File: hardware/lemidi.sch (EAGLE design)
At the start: 70 parts, among them Q1 IRLML6246, Q2 IRLML6246, Q3 IRLML6246, Q4 IRLML6246, Q5 si2305cd, U1 SPX5205 3v3, X3 debug, Y2 12MHz 0.25%, Y3 8MHz

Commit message: max5415
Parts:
- removed U$11: SJ_3P, Simplex-Jumpers:SJ_3P
- added C22: 100nF, rcl:C-EUC0805
- added J1: SJ_3P, Simplex-Jumpers:SJ_3P
- C18: value 100nF -> 1uF
- C19: value 4.7uF -> 100nF
- C2, C5: value 22pF -> 27pF
- R10, R6, R9: value 100k -> 47K
- U$9: value UBA-4R-D14T-4D -> USB-A
- Y2: value 12MHz 0.25% -> 12MHz 0.25% CL 16pF
- Y3: value 8MHz -> 8MHz CL 18pF
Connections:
- net TP5 renamed CS_J1
- removed net USB_ST1: R9.1, U$3.GPOUT3
- removed net USB_ST2: R10.1, U$3.GPOUT4
- removed net USB_ST3: R6.1, U$3.GPOUT2
- new net STATUS1: R6.1, U$3.GPOUT6
- new net STATUS2: R9.1, U$3.GPOUT7
- net +5V: now also C22.2, J1.2; no longer U$11.2
- net 5V_PC: now also U$10.15, U$10.8; no longer U$10.1, U$10.9
- net 5V_PC2: now also U$10.1, U$10.9; no longer U$10.15, U$10.8
- net GND: now also C22.1
- net N$10: now also J1.1; no longer U$11.1
- net N$23: now also J1.3; no longer U$11.3
- net SCLK: now also R10.1
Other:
- moved on the sheet: C1, C11, C12, C13, C14, C15, C16, C17, C18, C19, C20, C21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

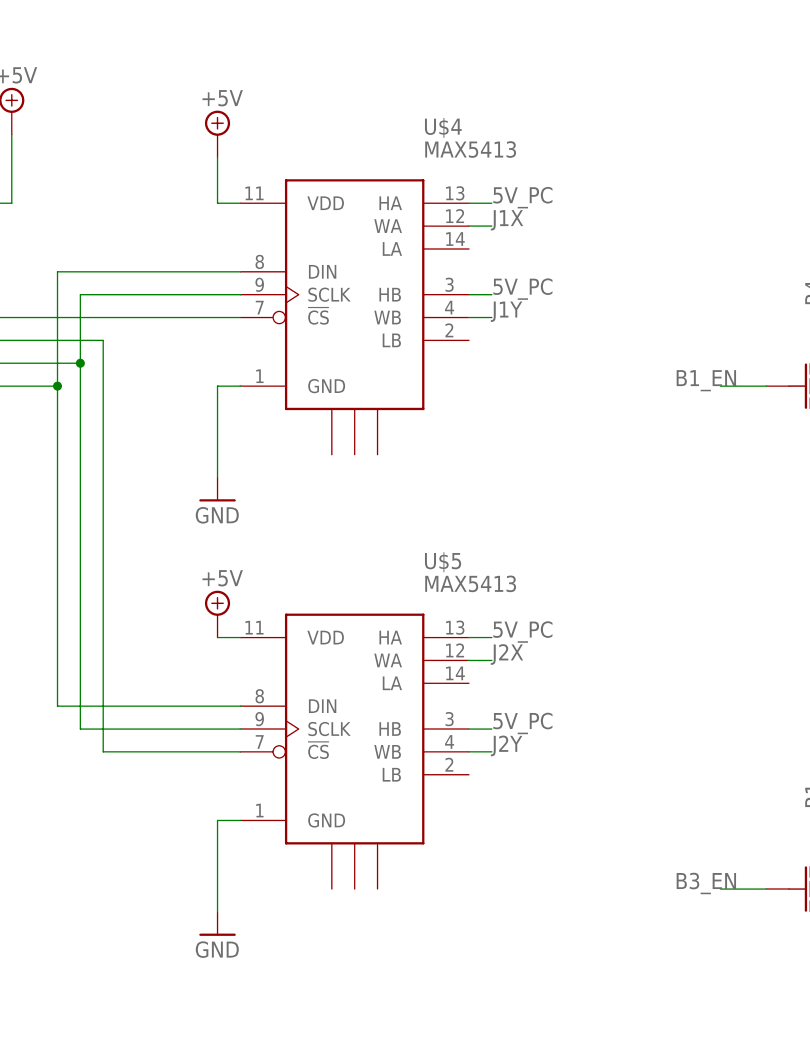
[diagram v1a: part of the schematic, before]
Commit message: switch to MCP42xxx digital pot
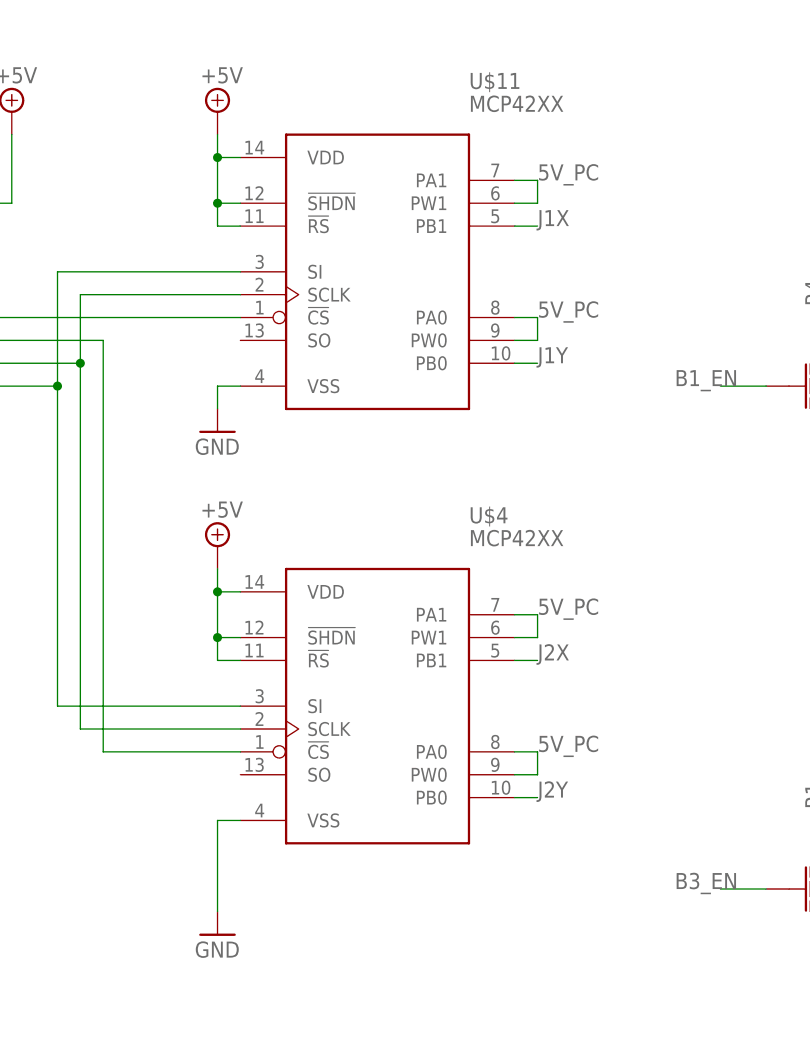
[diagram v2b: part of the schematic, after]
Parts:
- removed U$5: MAX5413, Simplex-ICs:MAX5413
- added U$11: MCP42XX, Simplex-ICs:MCP42XX
- U$4: value MAX5413 -> MCP42XX; device Simplex-ICs:MAX5413 -> Simplex-ICs:MCP42XX
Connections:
- net +5V: now also U$11.!RS, U$11.!SHDN, U$11.VDD, U$4.!RS, U$4.!SHDN; no longer U$5.VDD
- net 5V_PC: now also U$11.PA0, U$11.PA1, U$11.PW0, U$11.PW1, U$4.PA0, U$4.PA1, U$4.PW0, U$4.PW1; no longer U$4.HA, U$4.HB, U$5.HA, U$5.HB
- net GND: now also U$11.VSS, U$4.VSS; no longer U$4.GND, U$5.GND
- net HIGH_CS1: now also U$11.!CS; no longer U$4.!CS
- net HIGH_CS2: now also U$4.!CS; no longer U$5.!CS
- net HIGH_MOSI: now also U$11.SI, U$4.SI; no longer U$4.DIN, U$5.DIN
- net HIGH_SCLK: now also U$11.SCLK; no longer U$5.SCLK
- net J1X: now also U$11.PB1; no longer U$4.WA
- net J1Y: now also U$11.PB0; no longer U$4.WB
- net J2X: now also U$4.PB1; no longer U$5.WA
- net J2Y: now also U$4.PB0; no longer U$5.WB

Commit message: latest
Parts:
- U$11, U$4: value MCP42XX -> MCP42100
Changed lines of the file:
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@@
 <part name="C22" library="rcl" deviceset="C-EU" device="C0805" value="100nF"/>
 <part name="GND48" library="SparkFun" deviceset="GND" device=""/>
-<part name="U$11" library="Simplex-ICs" deviceset="MCP42XX" device=""/>
-<part name="U$4" library="Simplex-ICs" deviceset="MCP42XX" device=""/>
+<part name="U$11" library="Simplex-ICs" deviceset="MCP42XX" device="" value="MCP42100"/>
+<part name="U$4" library="Simplex-ICs" deviceset="MCP42XX" device="" value="MCP42100"/>
 </parts>
 <sheets>

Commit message: latest
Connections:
- net N$10: now also J1.3; no longer J1.1
- net N$23: now also J1.1; no longer J1.3
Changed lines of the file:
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@@
 <instance part="C13" gate="G$1" x="205.74" y="132.08" rot="R180"/>
 <instance part="GND29" gate="1" x="205.74" y="124.46"/>
-<instance part="J1" gate="G$1" x="48.26" y="198.12" rot="R270"/>
+<instance part="J1" gate="G$1" x="48.26" y="198.12" rot="MR270"/>
 <instance part="SUPPLY9" gate="+5V" x="48.26" y="210.82"/>
 <instance part="C14" gate="G$1" x="254" y="35.56" rot="R180"/>
@@
 <net name="N$10" class="0">
 <segment>
-<pinref part="J1" gate="G$1" pin="1"/>
-<wire x1="50.8" y1="203.2" x2="50.8" y2="205.74" width="0.1524" layer="91"/>
 <wire x1="50.8" y1="205.74" x2="55.88" y2="205.74" width="0.1524" layer="91"/>
 <pinref part="U$12" gate="G$1" pin="P$1"/>
+<pinref part="J1" gate="G$1" pin="3"/>
+<wire x1="50.8" y1="203.2" x2="50.8" y2="205.74" width="0.1524" layer="91"/>
 </segment>
 </net>
@@
 <segment>
 <pinref part="Q5" gate="G$1" pin="S"/>
-<pinref part="J1" gate="G$1" pin="3"/>
 <wire x1="40.64" y1="205.74" x2="45.72" y2="205.74" width="0.1524" layer="91"/>
-<wire x1="45.72" y1="205.74" x2="45.72" y2="203.2" width="0.1524" layer="91"/>
-</segment>
-</net>
+<pinref part="J1" gate="G$1" pin="1"/>
+<wire x1="45.72" y1="203.2" x2="45.72" y2="205.74" width="0.1524" layer="91"/>
+</segment>
+</net>

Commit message: rev 2
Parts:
- Q1, Q2, Q3, Q4: value IRLML6246 -> PMBF170
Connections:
- removed net B4: OK1D.COL, U$10.14
- removed net B4_EN: Q2.G, U$2.5
- removed net J2X: U$10.11, U$4.PB1
- removed net J2Y: U$10.13, U$4.PB0
- new net B0: OK1A.COL, U$10.2
- new net B0_EN: Q4.G, U$2.8
- new net J0X: U$10.3, U$11.PB1
- new net J0Y: U$10.6, U$11.PB0
- net +3V3: now also U$6.EN
- net B1: now also OK1B.COL, U$10.7; no longer OK1A.COL, U$10.2
- net B1_EN: now also Q3.G, U$2.7; no longer Q4.G, U$2.8
- net B2: now also OK1C.COL, U$10.10; no longer OK1B.COL, U$10.7
- net B2_EN: now also Q1.G, U$2.6; no longer Q3.G, U$2.7
- net B3: now also OK1D.COL, U$10.14; no longer OK1C.COL, U$10.10
- net B3_EN: now also Q2.G, U$2.5; no longer Q1.G, U$2.6
- net J1X: now also U$10.11, U$4.PB1; no longer U$10.3, U$11.PB1
- net J1Y: now also U$10.13, U$4.PB0; no longer U$10.6, U$11.PB0
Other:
- note added: "2.0"
- note removed: "2.1"
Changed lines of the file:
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@@
 <part name="+3V2" library="supply1" deviceset="+3V3" device=""/>
 <part name="OK1" library="optocoupler" deviceset="TLP283-4" device=""/>
-<part name="Q2" library="Simplex-DiscreteSemi" deviceset="MOSFET-NCHANNEL" device="_SOT23-3" value="IRLML6246"/>
+<part name="Q2" library="Simplex-DiscreteSemi" deviceset="MOSFET-NCHANNEL" device="_SOT23-3" value="PMBF170"/>
 <part name="R26" library="rcl" deviceset="R-EU_" device="R0805W" value="820"/>
 <part name="GND1" library="SparkFun" deviceset="GND" device=""/>
 <part name="GND3" library="SparkFun" deviceset="GND" device=""/>
-<part name="Q1" library="Simplex-DiscreteSemi" deviceset="MOSFET-NCHANNEL" device="_SOT23-3" value="IRLML6246"/>
+<part name="Q1" library="Simplex-DiscreteSemi" deviceset="MOSFET-NCHANNEL" device="_SOT23-3" value="PMBF170"/>
 <part name="R1" library="rcl" deviceset="R-EU_" device="R0805W" value="820"/>
 <part name="GND7" library="SparkFun" deviceset="GND" device=""/>
-<part name="Q3" library="Simplex-DiscreteSemi" deviceset="MOSFET-NCHANNEL" device="_SOT23-3" value="IRLML6246"/>
+<part name="Q3" library="Simplex-DiscreteSemi" deviceset="MOSFET-NCHANNEL" device="_SOT23-3" value="PMBF170"/>
 <part name="R3" library="rcl" deviceset="R-EU_" device="R0805W" value="820"/>
 <part name="GND8" library="SparkFun" deviceset="GND" device=""/>
-<part name="Q4" library="Simplex-DiscreteSemi" deviceset="MOSFET-NCHANNEL" device="_SOT23-3" value="IRLML6246"/>
+<part name="Q4" library="Simplex-DiscreteSemi" deviceset="MOSFET-NCHANNEL" device="_SOT23-3" value="PMBF170"/>
 <part name="R4" library="rcl" deviceset="R-EU_" device="R0805W" value="820"/>
 <part name="GND11" library="SparkFun" deviceset="GND" device=""/>
@@
 <sheet>
 <plain>
-<text x="449.58" y="7.62" size="3.81" layer="97">2.1</text>
+<text x="449.58" y="7.62" size="3.81" layer="97">2.0</text>
 <text x="30.48" y="53.34" size="1.778" layer="97">uC pins: 7 11 28</text>
 <text x="30.48" y="22.86" size="1.778" layer="97">digital output pins:
@@
 <wire x1="203.2" y1="203.2" x2="193.04" y2="203.2" width="0.1524" layer="91"/>
 <junction x="203.2" y="203.2"/>
+<pinref part="U$6" gate="G$1" pin="EN"/>
+<wire x1="208.28" y1="198.12" x2="203.2" y2="198.12" width="0.1524" layer="91"/>
+<wire x1="203.2" y1="198.12" x2="203.2" y2="203.2" width="0.1524" layer="91"/>
 </segment>
 <segment>
@@
 </segment>
 </net>
-<net name="B1_EN" class="0">
+<net name="B0_EN" class="0">
 <segment>
 <pinref part="Q4" gate="G$1" pin="G"/>
@@
 </segment>
 </net>
-<net name="B2_EN" class="0">
+<net name="B1_EN" class="0">
 <segment>
 <pinref part="Q3" gate="G$1" pin="G"/>
@@
 </segment>
 </net>
-<net name="B3_EN" class="0">
+<net name="B2_EN" class="0">
 <segment>
 <pinref part="Q1" gate="G$1" pin="G"/>
@@
 </segment>
 </net>
-<net name="B4_EN" class="0">
+<net name="B3_EN" class="0">
 <segment>
 <pinref part="Q2" gate="G$1" pin="G"/>
@@
 </segment>
 </net>
-<net name="B1" class="0">
+<net name="B0" class="0">
 <segment>
 <pinref part="OK1" gate="A" pin="COL"/>
@@
 </segment>
 </net>
-<net name="B2" class="0">
+<net name="B1" class="0">
 <segment>
 <pinref part="OK1" gate="B" pin="COL"/>
@@
 </segment>
 </net>
-<net name="B3" class="0">
+<net name="B2" class="0">
 <segment>
 <pinref part="OK1" gate="C" pin="COL"/>
@@
 </segment>
 </net>
-<net name="B4" class="0">
+<net name="B3" class="0">
 <segment>
 <pinref part="OK1" gate="D" pin="COL"/>
@@
 </segment>
 </net>
-<net name="J1X" class="0">
+<net name="J0X" class="0">
 <segment>
 <pinref part="U$10" gate="G$1" pin="3"/>
@@
 </segment>
 </net>
-<net name="J1Y" class="0">
+<net name="J0Y" class="0">
 <segment>
 <pinref part="U$10" gate="G$1" pin="6"/>
@@
 </segment>
 </net>
-<net name="J2X" class="0">
+<net name="J1X" class="0">
 <segment>
 <pinref part="U$10" gate="G$1" pin="11"/>
@@
 </segment>
 </net>
-<net name="J2Y" class="0">
+<net name="J1Y" class="0">
 <segment>
 <pinref part="U$10" gate="G$1" pin="13"/>
